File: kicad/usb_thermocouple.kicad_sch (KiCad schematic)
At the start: 4 parts

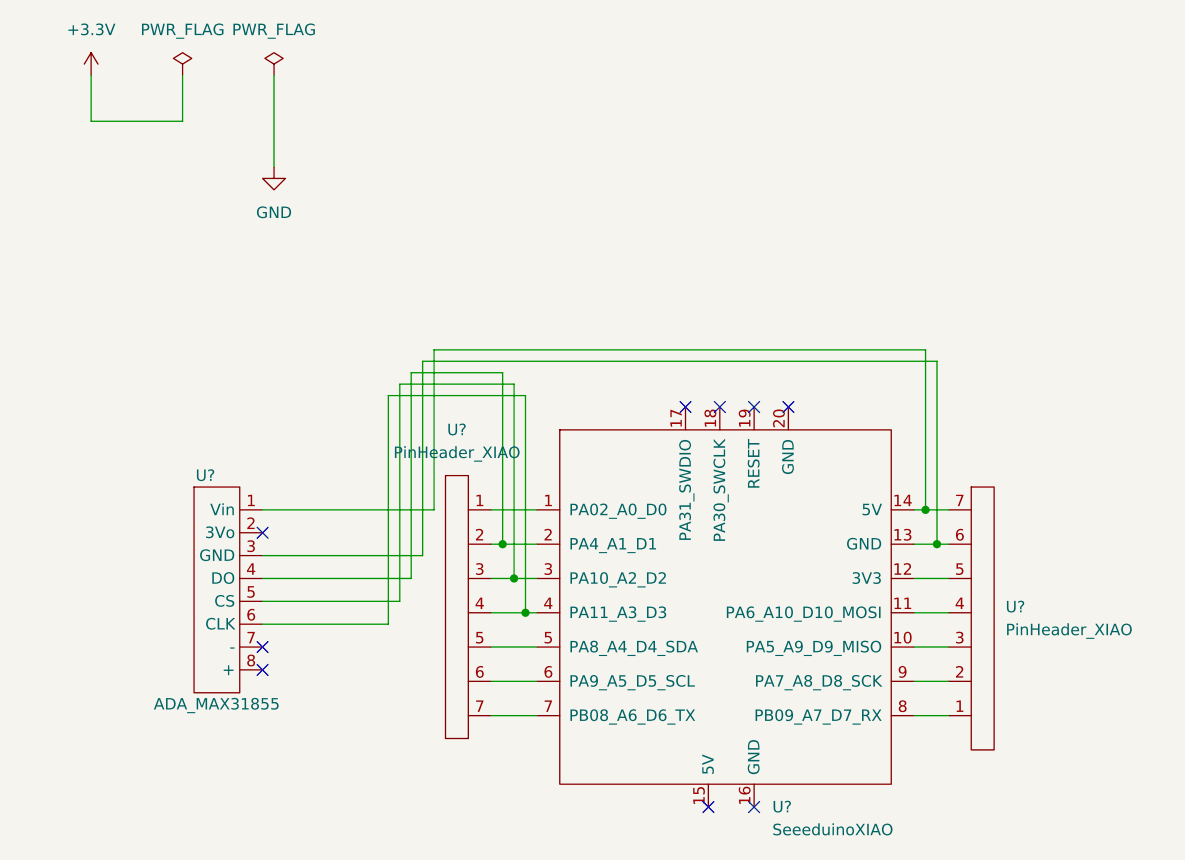
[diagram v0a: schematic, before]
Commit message: 3V3のPWE_FLGを削除した
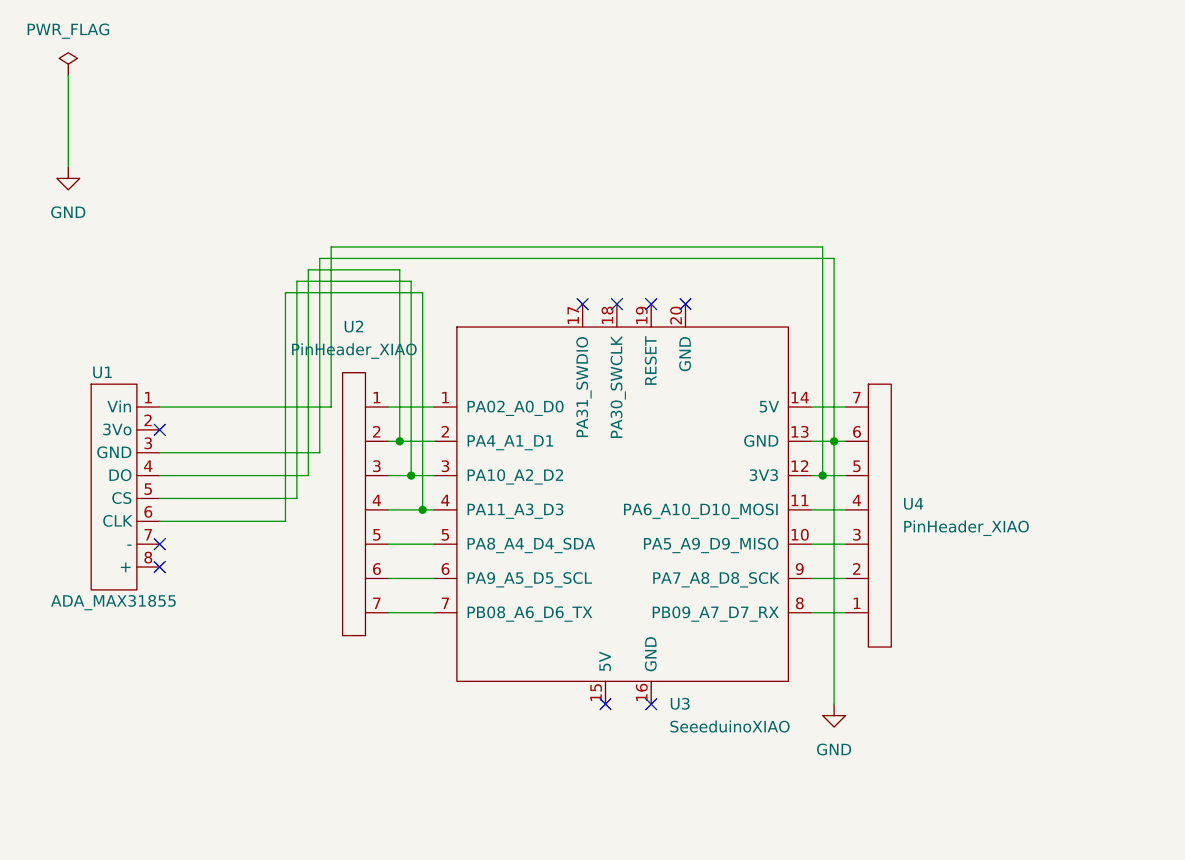
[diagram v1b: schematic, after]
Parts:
- U1: renamed from U?; footprint (none) -> KICAD_MYLIB:ADA_MAX31855
- U2, U4: renamed from U?; footprint (none) -> KICAD_MYLIB:PinHeader_XIAO
- U3: renamed from U?; footprint (none) -> XIAO:Seeeduino XIAO-MOUDLE14P-2.54-21X17.8MM
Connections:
- net GND: now also U1.3 (GND), U3.13 (GND), U4.6
- net at U3.14 (5V), U4.7: no longer U1.1 (Vin)
- net at U3.12 (3V3), U4.5: now also U1.1 (Vin)
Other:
- moved on the sheet: U1, U2, U3, U4

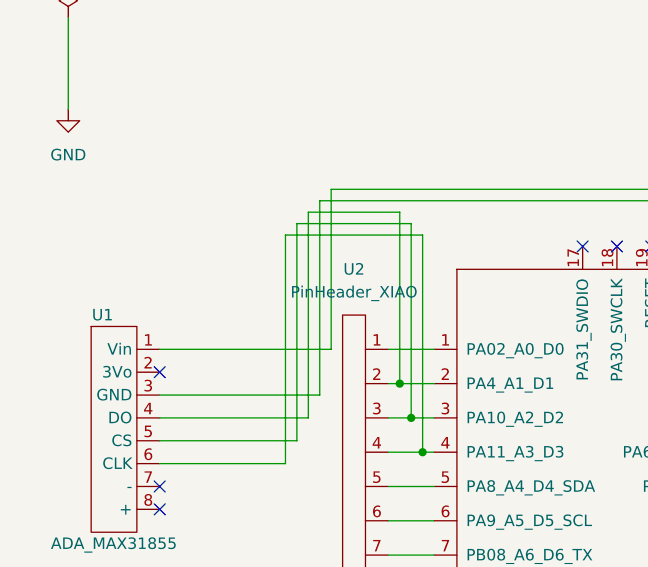
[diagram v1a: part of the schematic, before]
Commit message: XIAOの3.3V出力をVin→3Voに接続しなおした ERC OK
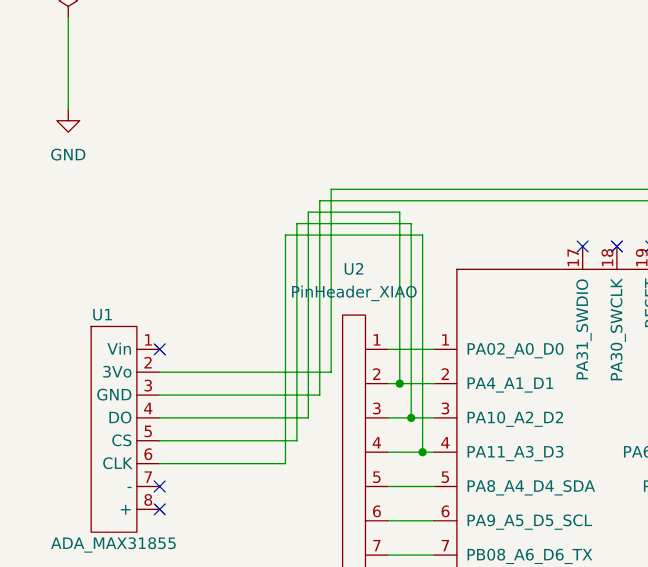
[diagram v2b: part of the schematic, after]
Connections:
- net at U3.12 (3V3), U4.5: now also U1.2 (3Vo); no longer U1.1 (Vin)
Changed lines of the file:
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@@
   (junction (at 99.06 62.23) (diameter 0) (color 0 0 0 0)
   )
-  (no_connect (at 25.4 57.15))
   (no_connect (at 74.93 87.63))
   (no_connect (at 80.01 87.63))
@@
   (no_connect (at 80.01 43.18))
   (no_connect (at 72.39 43.18))
+  (no_connect (at 25.4 54.61))
   (no_connect (at 25.4 69.85))
   (no_connect (at 25.4 72.39))
-  (wire (pts (xy 44.45 36.83) (xy 44.45 54.61))
+  (wire (pts (xy 44.45 36.83) (xy 44.45 57.15))
     (stroke (width 0) (type default) (color 0 0 0 0))
   )
@@
   )
   (wire (pts (xy 52.07 39.37) (xy 52.07 58.42))
-    (stroke (width 0) (type default) (color 0 0 0 0))
-  )
-  (wire (pts (xy 44.45 54.61) (xy 25.4 54.61))
     (stroke (width 0) (type default) (color 0 0 0 0))
   )
@@
     (stroke (width 0) (type default) (color 0 0 0 0))
   )
+  (wire (pts (xy 44.45 57.15) (xy 25.4 57.15))
+    (stroke (width 0) (type default) (color 0 0 0 0))
+  )

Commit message: XIAOのフットプリントを変更
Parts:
- U3: footprint XIAO:Seeeduino XIAO-MOUDLE14P-2.54-21X17.8MM -> KICAD_MYLIB:SeeedXIAO
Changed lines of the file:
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@@
       (effects (font (size 1.27 1.27)) (justify left))
     )
-    (property "Footprint" "XIAO:Seeeduino XIAO-MOUDLE14P-2.54-21X17.8MM" (id 2) (at 68.58 60.96 0)
+    (property "Footprint" "KICAD_MYLIB:SeeedXIAO" (id 2) (at 68.58 60.96 0)
       (effects (font (size 1.27 1.27)) hide)
     )
@@
     )
     (path "/86e9f412-5543-43e1-bba0-b970b0e0f286"
-      (reference "U3") (unit 1) (value "SeeeduinoXIAO") (footprint "XIAO:Seeeduino XIAO-MOUDLE14P-2.54-21X17.8MM")
+      (reference "U3") (unit 1) (value "SeeeduinoXIAO") (footprint "KICAD_MYLIB:SeeedXIAO")
     )
     (path "/c63609db-2775-4841-b251-3f58a4aac31c"

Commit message: ユニット番号を変更
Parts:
- renumbered U3 to U1, U1 to U2, U2 to U3
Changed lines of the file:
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@@
   (symbol (lib_id "KICAD_MYLIB:ADA_MAX31855") (at 17.78 74.93 0) (unit 1)
     (in_bom yes) (on_board yes)
-    (property "Reference" "U1" (id 0) (at 19.05 50.8 0))
+    (property "Reference" "U2" (id 0) (at 19.05 50.8 0))
     (property "Value" "ADA_MAX31855" (id 1) (at 20.32 76.2 0))
     (property "Footprint" "KICAD_MYLIB:ADA_MAX31855" (id 2) (at 13.97 52.07 0)
@@
   (symbol (lib_id "XIAO:SeeeduinoXIAO") (at 77.47 66.04 0) (unit 1)
     (in_bom yes) (on_board yes) (fields_autoplaced)
-    (property "Reference" "U3" (id 0) (at 82.0294 87.63 0)
+    (property "Reference" "U1" (id 0) (at 82.0294 87.63 0)
       (effects (font (size 1.27 1.27)) (justify left))
     )
@@
   (symbol (lib_id "KICAD_MYLIB:PinHeader_XIAO") (at 48.26 50.8 180) (unit 1)
     (in_bom yes) (on_board yes) (fields_autoplaced)
-    (property "Reference" "U2" (id 0) (at 46.99 45.72 0))
+    (property "Reference" "U3" (id 0) (at 46.99 45.72 0))
     (property "Value" "PinHeader_XIAO" (id 1) (at 46.99 48.26 0))
     (property "Footprint" "KICAD_MYLIB:PinHeader_XIAO" (id 2) (at 46.99 82.55 0)
@@
       (reference "#PWR0103") (unit 1) (value "GND") (footprint "")
     )
+    (path "/86e9f412-5543-43e1-bba0-b970b0e0f286"
+      (reference "U1") (unit 1) (value "SeeeduinoXIAO") (footprint "KICAD_MYLIB:SeeedXIAO")
+    )
     (path "/0915160e-514e-4927-a996-9bf411d8fb26"
-      (reference "U1") (unit 1) (value "ADA_MAX31855") (footprint "KICAD_MYLIB:ADA_MAX31855")
+      (reference "U2") (unit 1) (value "ADA_MAX31855") (footprint "KICAD_MYLIB:ADA_MAX31855")
     )
     (path "/efff797f-80ba-43d4-82d8-1094df15cadd"
-      (reference "U2") (unit 1) (value "PinHeader_XIAO") (footprint "KICAD_MYLIB:PinHeader_XIAO")
-    )
-    (path "/86e9f412-5543-43e1-bba0-b970b0e0f286"
-      (reference "U3") (unit 1) (value "SeeeduinoXIAO") (footprint "KICAD_MYLIB:SeeedXIAO")
+      (reference "U3") (unit 1) (value "PinHeader_XIAO") (footprint "KICAD_MYLIB:PinHeader_XIAO")
     )
     (path "/c63609db-2775-4841-b251-3f58a4aac31c"
